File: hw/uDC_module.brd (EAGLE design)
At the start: 25 x 45 mm, 37 parts, among them J1 GROVE-4P-2.0-3470130P1, J2 GROVE-4P-2.0-3470130P1, U5 LD3985XX, X1 22-23-2021, X2 22-23-2021, X3 53047-06, X4 53047-06

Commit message: working on signal routin
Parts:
- added ZD1: (no value), dp_devices:SOD-323F
- moved C13 2.25 mm to (9.10, 22.9), turned to 0 degrees
- moved C18 0.30 mm to (5.80, 19.2)
- moved U5 0.20 mm to (5.80, 16.3)
- moved R2 0.10 mm to (12.7, 23.7)
- moved C15 0.10 mm to (11.3, 23.7)
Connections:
- removed net INV: U$7.P$7
- net !D2: now also U$6.33
- net !SF: now also U$6.31
- net D1: now also U$6.32
- net EN: now also U$6.18
- net FB: now also U$6.19, ZD1.C
- net GND: now also ZD1.A
- net IN1: now also U$6.26
- net IN2: now also U$6.29
- net SLEW: now also U$6.25
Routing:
- net !D2: track 0.00 -> 37.8 mm, vias 0 -> 2
- net D1: track 0.00 -> 28.6 mm, vias 0 -> 2
- net !SF: track 1.10 -> 29.7 mm, vias 1 -> 2
- net IN2: track 0.00 -> 12.2 mm, vias 0 -> 2
- net IN1: track 0.00 -> 10.4 mm
- net SLEW: track 0.00 -> 9.51 mm
- net EN: track 0.00 -> 8.76 mm
- net FB: track 3.25 -> 9.42 mm

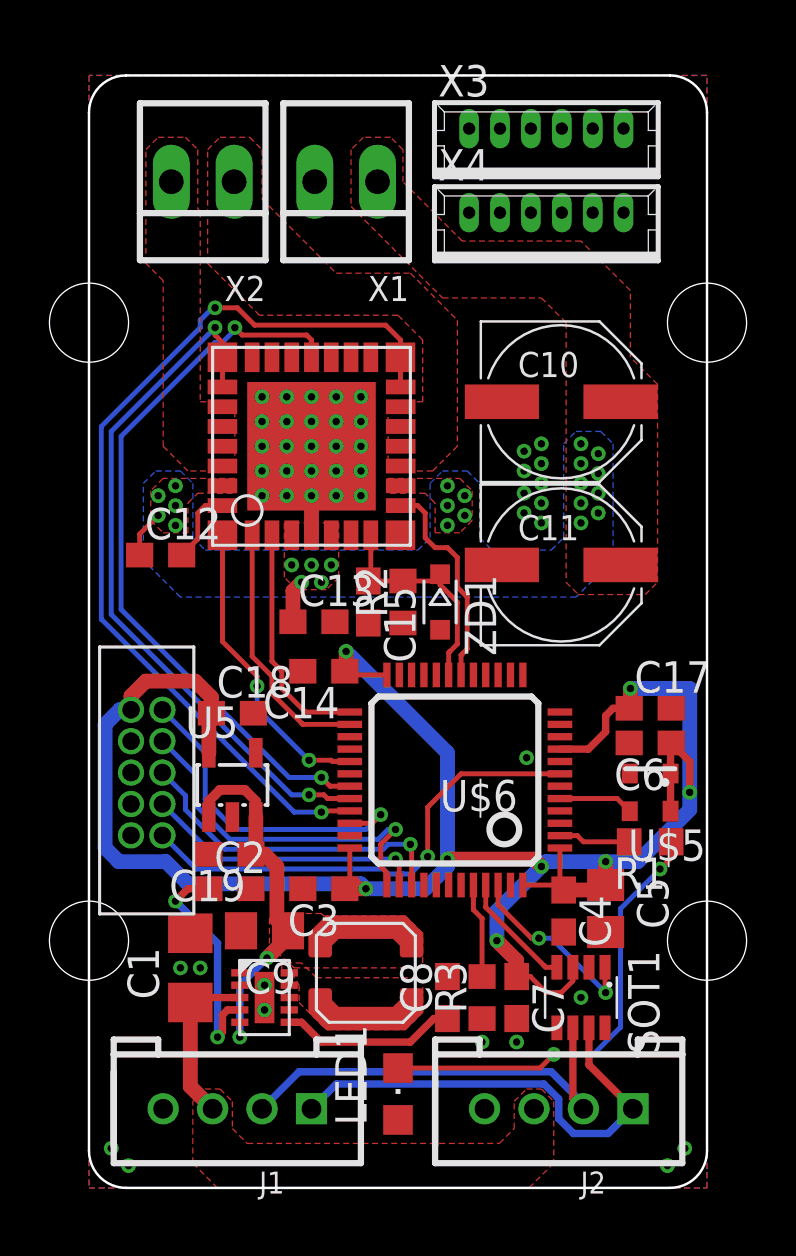
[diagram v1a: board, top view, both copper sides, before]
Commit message: routing encoder signals
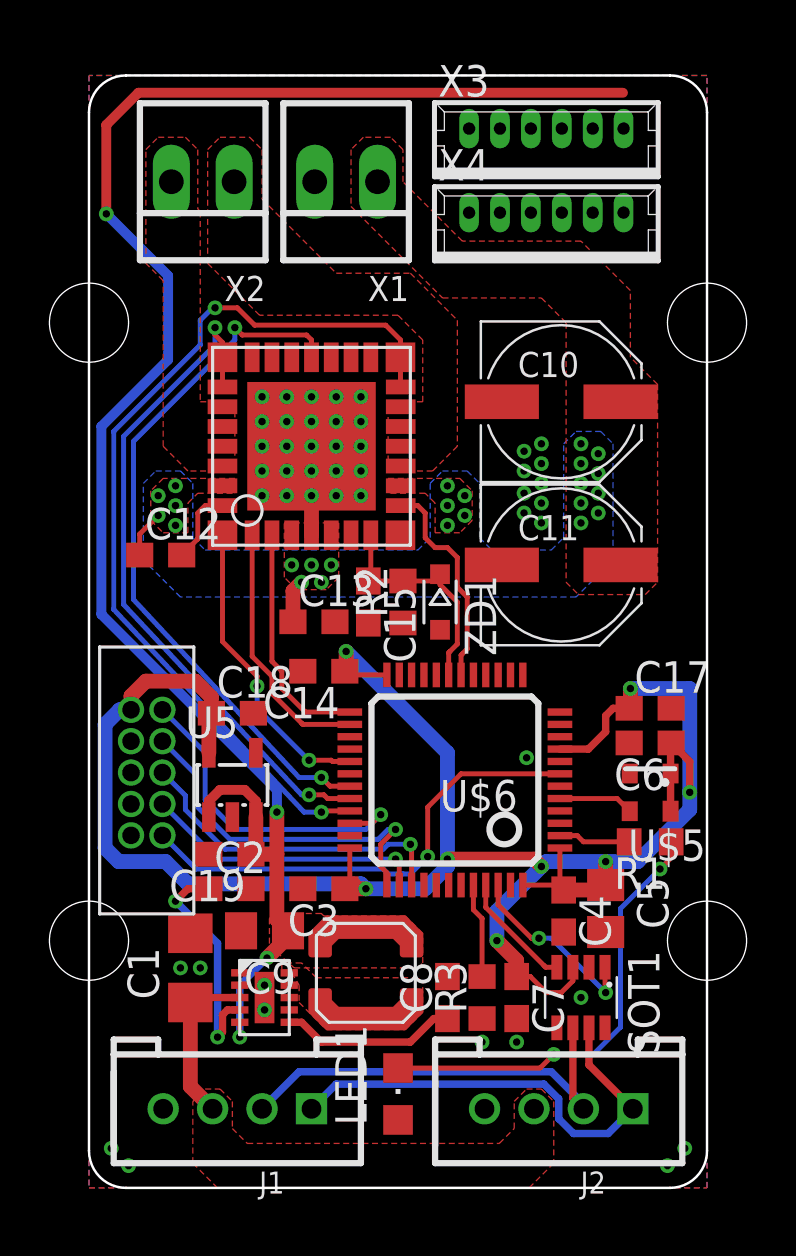
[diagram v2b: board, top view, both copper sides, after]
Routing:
- net +5V: track 14.9 -> 71.2 mm, vias 2 -> 4
- net !SF: track 29.7 -> 28.7 mm
- net !D2: track 37.8 -> 37.0 mm
- net D1: track 28.6 -> 27.8 mm
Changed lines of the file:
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@@
 <grid distance="0.5" unitdist="mm" unit="mm" style="dots" multiple="1" display="yes" altdistance="0.1" altunitdist="mm" altunit="mm"/>
 <layers>
-<layer number="1" name="Top" color="4" fill="1" visible="no" active="yes"/>
+<layer number="1" name="Top" color="4" fill="1" visible="yes" active="yes"/>
 <layer number="16" name="Bottom" color="1" fill="1" visible="yes" active="yes"/>
 <layer number="17" name="Pads" color="2" fill="1" visible="yes" active="yes"/>
@@
 <layer number="42" name="bRestrict" color="1" fill="10" visible="yes" active="yes"/>
 <layer number="43" name="vRestrict" color="2" fill="10" visible="no" active="yes"/>
-<layer number="44" name="Drills" color="7" fill="1" visible="no" active="yes"/>
-<layer number="45" name="Holes" color="7" fill="1" visible="yes" active="yes"/>
-<layer number="46" name="Milling" color="3" fill="1" visible="yes" active="yes"/>
+<layer number="44" name="Drills" color="7" fill="1" visible="yes" active="yes"/>
+<layer number="45" name="Holes" color="7" fill="1" visible="no" active="yes"/>
+<layer number="46" name="Milling" color="3" fill="1" visible="no" active="yes"/>
 <layer number="47" name="Measures" color="7" fill="1" visible="no" active="yes"/>
 <layer number="48" name="Document" color="7" fill="1" visible="no" active="yes"/>
@@
 <wire x1="10.55" y1="16.25" x2="9.75" y2="16.25" width="0.2" layer="1"/>
 <wire x1="9.75" y1="16.25" x2="9.4" y2="16.6" width="0.2" layer="1"/>
-<wire x1="1.3" y1="23.4" x2="1.3" y2="30.4" width="0.2" layer="16"/>
-<wire x1="1.3" y1="30.4" x2="5.1" y2="34.2" width="0.2" layer="16"/>
-<wire x1="5.9" y1="34.8" x2="5.9" y2="34.7" width="0.2" layer="16"/>
-<wire x1="5.9" y1="34.7" x2="5.4" y2="34.2" width="0.2" layer="16"/>
-<wire x1="5.4" y1="34.2" x2="5.1" y2="34.2" width="0.2" layer="16"/>
-<wire x1="1.3" y1="23.4" x2="8.1" y2="16.6" width="0.2" layer="16"/>
-<wire x1="8.1" y1="16.6" x2="9.4" y2="16.6" width="0.2" layer="16"/>
+<wire x1="1.8" y1="23.8" x2="1.8" y2="30.2" width="0.2" layer="16"/>
+<wire x1="1.8" y1="23.8" x2="8.5" y2="16.6" width="0.2" layer="16"/>
+<wire x1="8.5" y1="16.6" x2="9.4" y2="16.6" width="0.2" layer="16"/>
+<wire x1="1.8" y1="30.2" x2="5.9" y2="34.3" width="0.2" layer="16"/>
+<wire x1="5.9" y1="34.3" x2="5.9" y2="34.8" width="0.2" layer="16"/>
 </signal>
 <signal name="SLEW">
@@
 <wire x1="10.55" y1="15.25" x2="9.45" y2="15.25" width="0.2" layer="1"/>
 <wire x1="9.45" y1="15.25" x2="9.4" y2="15.2" width="0.2" layer="1"/>
-<wire x1="0.5" y1="30.8" x2="4.5" y2="34.8" width="0.2" layer="16"/>
-<wire x1="4.5" y1="34.8" x2="4.5" y2="35.1" width="0.2" layer="16"/>
-<wire x1="5.1" y1="35.6" x2="5" y2="35.6" width="0.2" layer="16"/>
-<wire x1="5" y1="35.6" x2="4.5" y2="35.1" width="0.2" layer="16"/>
-<wire x1="0.5" y1="23" x2="0.5" y2="30.8" width="0.2" layer="16"/>
-<wire x1="0.5" y1="23" x2="8.3" y2="15.2" width="0.2" layer="16"/>
-<wire x1="8.3" y1="15.2" x2="9.4" y2="15.2" width="0.2" layer="16"/>
+<wire x1="1" y1="23.4" x2="1" y2="30.6" width="0.2" layer="16"/>
+<wire x1="1" y1="23.4" x2="8.7" y2="15.2" width="0.2" layer="16"/>
+<wire x1="8.7" y1="15.2" x2="9.4" y2="15.2" width="0.2" layer="16"/>
+<wire x1="1" y1="30.6" x2="4.5" y2="34.1" width="0.2" layer="16"/>
+<wire x1="4.5" y1="34.1" x2="4.5" y2="35.1" width="0.2" layer="16"/>
+<wire x1="4.5" y1="35.1" x2="5" y2="35.6" width="0.2" layer="16"/>
+<wire x1="5" y1="35.6" x2="5.1" y2="35.6" width="0.2" layer="16"/>
 </signal>
 <signal name="IN2">
@@
 <wire x1="6.75" y1="15.65" x2="6.3" y2="16.1" width="0.4" layer="1"/>
 <wire x1="6.3" y1="16.1" x2="5.3" y2="16.1" width="0.4" layer="1"/>
-<wire x1="6.55" y1="13.5" x2="7.1" y2="13.5" width="0.6" layer="1"/>
-<wire x1="7.1" y1="13.5" x2="7.6" y2="13" width="0.6" layer="1"/>
-<wire x1="7.6" y1="13" x2="7.6" y2="10.85" width="0.6" layer="1"/>
 <wire x1="7.6" y1="10.85" x2="8.05" y2="10.4" width="0.6" layer="1"/>
+<wire x1="7.6" y1="10.85" x2="7.6" y2="13.5" width="0.6" layer="1"/>
+<via x="7.6" y="15.2" extent="1-16" drill="0.3"/>
+<wire x1="7.6" y1="13.5" x2="7.6" y2="15.2" width="0.6" layer="1"/>
+<wire x1="6.55" y1="13.5" x2="7.6" y2="13.5" width="0.6" layer="1"/>
+<wire x1="7.6" y1="15.2" x2="7.6" y2="16.1" width="0.4" layer="16"/>
+<wire x1="7.6" y1="16.1" x2="0.5" y2="23.2" width="0.4" layer="16"/>
+<wire x1="0.5" y1="23.2" x2="0.5" y2="30.8" width="0.4" layer="16"/>
+<wire x1="0.5" y1="30.8" x2="3.2" y2="33.5" width="0.4" layer="16"/>
+<wire x1="3.2" y1="33.5" x2="3.2" y2="36.9" width="0.4" layer="16"/>
+<wire x1="3.2" y1="36.9" x2="0.7" y2="39.4" width="0.4" layer="16"/>
+<via x="0.7" y="39.4" extent="1-16" drill="0.3"/>
+<wire x1="0.7" y1="39.4" x2="0.7" y2="43" width="0.4" layer="1"/>
+<wire x1="0.7" y1="43" x2="2" y2="44.3" width="0.4" layer="1"/>
+<wire x1="2" y1="44.3" x2="21.6" y2="44.3" width="0.4" layer="1"/>
 </signal>
 <signal name="D1">
@@
 <wire x1="9.65" y1="15.75" x2="9.5" y2="15.9" width="0.2" layer="1"/>
 <wire x1="9.5" y1="15.9" x2="8.9" y2="15.9" width="0.2" layer="1"/>
-<wire x1="0.9" y1="23.2" x2="0.9" y2="30.6" width="0.2" layer="16"/>
-<wire x1="0.9" y1="30.6" x2="5.1" y2="34.8" width="0.2" layer="16"/>
-<wire x1="0.9" y1="23.2" x2="8.2" y2="15.9" width="0.2" layer="16"/>
-<wire x1="8.2" y1="15.9" x2="8.9" y2="15.9" width="0.2" layer="16"/>
+<wire x1="1.4" y1="23.6" x2="1.4" y2="30.4" width="0.2" layer="16"/>
+<wire x1="1.4" y1="23.6" x2="8.6" y2="15.9" width="0.2" layer="16"/>
+<wire x1="8.6" y1="15.9" x2="8.9" y2="15.9" width="0.2" layer="16"/>
+<wire x1="1.4" y1="30.4" x2="5.1" y2="34.1" width="0.2" layer="16"/>
+<wire x1="5.1" y1="34.1" x2="5.1" y2="34.8" width="0.2" layer="16"/>
 </signal>
 </signals>

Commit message: layout completed
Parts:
- moved X3 3.40 mm to (18.5, 39.0)
- moved X4 3.40 mm to (18.5, 42.4)
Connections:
- new net ANALOG: U$6.12, X4.6
- new net ENC_A: U$6.42, X4.3
- new net ENC_B: U$6.43, X4.4
- new net ENC_I: U$6.41, X4.5
- new net LIMIT_A: U$6.13, X3.1
- new net LIMIT_B: U$6.14, X3.3
- new net STOP: U$6.15, X3.5
- net +5V: now also X4.1
- net GND: now also X3.2, X3.4, X3.6, X4.2
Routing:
- net ENC_B: track 0.00 -> 45.7 mm, vias 0 -> 1
- net ENC_I: track 0.00 -> 44.1 mm, vias 0 -> 1
- net ENC_A: track 0.00 -> 43.7 mm, vias 0 -> 1
- net ANALOG: track 0.00 -> 34.6 mm, vias 0 -> 1
- net STOP: track 0.00 -> 26.0 mm, vias 0 -> 1
- net LIMIT_B: track 0.00 -> 25.9 mm, vias 0 -> 1
- net LIMIT_A: track 0.00 -> 25.0 mm, vias 0 -> 1
- net +3V3: track 86.7 -> 83.3 mm
- net +5V: track 71.2 -> 72.3 mm
- net GND: vias 46 -> 53
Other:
- board text added: "ENC"
- board text added: "MOTOR"
- board text added: "STOP"
- board text added: "SUPPLY"

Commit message: updated all connectors to have GND on pin 1
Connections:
- net +5V: now also X4.2; no longer X4.1
- net GND: now also X3.1, X3.3, X3.5, X4.1; no longer X3.2, X3.4, X3.6, X4.2
- net LIMIT_A: now also X3.2; no longer X3.1
- net LIMIT_B: now also X3.4; no longer X3.3
- net STOP: now also X3.6; no longer X3.5
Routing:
- net +5V: track 72.3 -> 71.1 mm
- net LIMIT_A: track 25.0 -> 24.4 mm
- net STOP: track 26.0 -> 26.5 mm
- net LIMIT_B: track 25.9 -> 26.4 mm
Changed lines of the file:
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@@
 <grid distance="0.5" unitdist="mm" unit="mm" style="dots" multiple="1" display="yes" altdistance="0.1" altunitdist="mm" altunit="mm"/>
 <layers>
-<layer number="1" name="Top" color="4" fill="1" visible="yes" active="yes"/>
-<layer number="16" name="Bottom" color="1" fill="1" visible="no" active="yes"/>
+<layer number="1" name="Top" color="4" fill="1" visible="no" active="yes"/>
+<layer number="16" name="Bottom" color="1" fill="1" visible="yes" active="yes"/>
 <layer number="17" name="Pads" color="2" fill="1" visible="yes" active="yes"/>
 <layer number="18" name="Vias" color="2" fill="1" visible="yes" active="yes"/>
 <layer number="19" name="Unrouted" color="6" fill="1" visible="yes" active="yes"/>
 <layer number="20" name="Dimension" color="15" fill="1" visible="yes" active="yes"/>
-<layer number="21" name="tPlace" color="7" fill="1" visible="yes" active="yes"/>
-<layer number="22" name="bPlace" color="7" fill="1" visible="no" active="yes"/>
-<layer number="23" name="tOrigins" color="15" fill="1" visible="yes" active="yes"/>
-<layer number="24" name="bOrigins" color="15" fill="1" visible="no" active="yes"/>
+<layer number="21" name="tPlace" color="7" fill="1" visible="no" active="yes"/>
+<layer number="22" name="bPlace" color="7" fill="1" visible="yes" active="yes"/>
+<layer number="23" name="tOrigins" color="15" fill="1" visible="no" active="yes"/>
+<layer number="24" name="bOrigins" color="15" fill="1" visible="yes" active="yes"/>
 <layer number="25" name="tNames" color="7" fill="1" visible="no" active="yes"/>
 <layer number="26" name="bNames" color="7" fill="1" visible="no" active="yes"/>
@@
 <layer number="37" name="tTest" color="7" fill="1" visible="no" active="yes"/>
 <layer number="38" name="bTest" color="7" fill="1" visible="no" active="yes"/>
-<layer number="39" name="tKeepout" color="4" fill="11" visible="yes" active="yes"/>
-<layer number="40" name="bKeepout" color="1" fill="11" visible="no" active="yes"/>
-<layer number="41" name="tRestrict" color="4" fill="10" visible="yes" active="yes"/>
-<layer number="42" name="bRestrict" color="1" fill="10" visible="no" active="yes"/>
+<layer number="39" name="tKeepout" color="4" fill="11" visible="no" active="yes"/>
+<layer number="40" name="bKeepout" color="1" fill="11" visible="yes" active="yes"/>
+<layer number="41" name="tRestrict" color="4" fill="10" visible="no" active="yes"/>
+<layer number="42" name="bRestrict" color="1" fill="10" visible="yes" active="yes"/>
 <layer number="43" name="vRestrict" color="2" fill="10" visible="no" active="yes"/>
 <layer number="44" name="Drills" color="7" fill="1" visible="no" active="yes"/>
@@
 <layer number="46" name="Milling" color="3" fill="1" visible="yes" active="yes"/>
 <layer number="47" name="Measures" color="7" fill="1" visible="no" active="yes"/>
-<layer number="48" name="Document" color="7" fill="1" visible="yes" active="yes"/>
+<layer number="48" name="Document" color="7" fill="1" visible="no" active="yes"/>
 <layer number="49" name="Reference" color="7" fill="1" visible="no" active="yes"/>
 <layer number="50" name="dxf" color="7" fill="1" visible="no" active="no"/>
-<layer number="51" name="tDocu" color="7" fill="1" visible="yes" active="yes"/>
-<layer number="52" name="bDocu" color="7" fill="1" visible="no" active="yes"/>
+<layer number="51" name="tDocu" color="7" fill="1" visible="no" active="yes"/>
+<layer number="52" name="bDocu" color="7" fill="1" visible="yes" active="yes"/>
 <layer number="53" name="tGND_GNDA" color="7" fill="1" visible="no" active="no"/>
 <layer number="54" name="bGND_GNDA" color="7" fill="1" visible="no" active="no"/>
@@
 <wire x1="9" y1="26.4" x2="9" y2="28" width="0.6" layer="1"/>
 <contactref element="ZD1" pad="A"/>
-<contactref element="X4" pad="2"/>
-<contactref element="X3" pad="2"/>
-<contactref element="X3" pad="4"/>
-<contactref element="X3" pad="6"/>
 <via x="4.5" y="23.2" extent="1-16" drill="0.3"/>
 <via x="4.5" y="22.2" extent="1-16" drill="0.3"/>
@@
 <via x="17.3" y="22.9" extent="1-16" drill="0.3"/>
 <via x="18.1" y="11.2" extent="1-16" drill="0.3"/>
+<contactref element="X4" pad="1"/>
+<contactref element="X3" pad="1"/>
+<contactref element="X3" pad="3"/>
+<contactref element="X3" pad="5"/>
 </signal>
 <signal name="VIN">
@@
 <wire x1="0.7" y1="39.4" x2="0.7" y2="43" width="0.4" layer="1"/>
 <wire x1="0.7" y1="43" x2="2" y2="44.3" width="0.4" layer="1"/>
-<wire x1="2" y1="44.3" x2="20.1" y2="44.3" width="0.4" layer="1"/>
-<contactref element="X4" pad="1"/>
-<wire x1="20.1" y1="44.3" x2="21" y2="44.3" width="0.4" layer="1"/>
-<wire x1="21.625" y1="42.85" x2="21.625" y2="43.675" width="0.4" layer="1"/>
-<wire x1="21.625" y1="43.675" x2="21" y2="44.3" width="0.4" layer="1"/>
+<contactref element="X4" pad="2"/>
+<wire x1="20.375" y1="42.85" x2="20.375" y2="43.625" width="0.4" layer="1"/>
+<wire x1="20.375" y1="43.625" x2="19.7" y2="44.3" width="0.4" layer="1"/>
+<wire x1="19.7" y1="44.3" x2="2" y2="44.3" width="0.4" layer="1"/>
 </signal>
 <signal name="D1">
@@
 </signal>
 <signal name="STOP">
-<contactref element="X3" pad="5"/>
 <contactref element="U$6" pad="15"/>
 <via x="16.3" y="19.7" extent="1-16" drill="0.3"/>
 <wire x1="16.55" y1="20.75" x2="16.55" y2="19.95" width="0.2" layer="1"/>
 <wire x1="16.55" y1="19.95" x2="16.3" y2="19.7" width="0.2" layer="1"/>
-<wire x1="16.625" y1="39.45" x2="16.625" y2="38.675" width="0.2" layer="16"/>
-<wire x1="16.625" y1="38.675" x2="19.4" y2="35.9" width="0.2" layer="16"/>
-<wire x1="19.4" y1="35.9" x2="19.4" y2="32.5" width="0.2" layer="16"/>
 <wire x1="19.4" y1="32.5" x2="22.1" y2="29.8" width="0.2" layer="16"/>
 <wire x1="22.1" y1="29.8" x2="22.1" y2="24.9" width="0.2" layer="16"/>
@@
 <wire x1="16.3" y1="19.8" x2="17.2" y2="20.7" width="0.2" layer="16"/>
 <wire x1="17.2" y1="20.7" x2="17.9" y2="20.7" width="0.2" layer="16"/>
+<contactref element="X3" pad="6"/>
+<wire x1="19.4" y1="32.5" x2="19.4" y2="34.6" width="0.2" layer="16"/>
+<wire x1="15.375" y1="39.45" x2="15.375" y2="38.625" width="0.2" layer="16"/>
+<wire x1="15.375" y1="38.625" x2="19.4" y2="34.6" width="0.2" layer="16"/>
 </signal>
 <signal name="LIMIT_B">
-<contactref element="X3" pad="3"/>
 <contactref element="U$6" pad="14"/>
 <via x="17" y="19.2" extent="1-16" drill="0.3"/>
 <wire x1="17.05" y1="20.75" x2="17.05" y2="19.25" width="0.2" layer="1"/>
 <wire x1="17.05" y1="19.25" x2="17" y2="19.2" width="0.2" layer="1"/>
-<wire x1="19.125" y1="39.45" x2="19.125" y2="38.675" width="0.2" layer="16"/>
-<wire x1="19.125" y1="38.675" x2="19.8" y2="38" width="0.2" layer="16"/>
-<wire x1="19.8" y1="38" x2="19.8" y2="32.7" width="0.2" layer="16"/>
 <wire x1="19.8" y1="32.7" x2="22.5" y2="30" width="0.2" layer="16"/>
 <wire x1="17" y1="19.2" x2="17" y2="19.9" width="0.2" layer="16"/>
@@
 <wire x1="18.1" y1="20.3" x2="22.5" y2="24.7" width="0.2" layer="16"/>
 <wire x1="22.5" y1="24.7" x2="22.5" y2="30" width="0.2" layer="16"/>
+<contactref element="X3" pad="4"/>
+<wire x1="19.8" y1="32.7" x2="19.8" y2="36.7" width="0.2" layer="16"/>
+<wire x1="17.875" y1="39.45" x2="17.875" y2="38.625" width="0.2" layer="16"/>
+<wire x1="17.875" y1="38.625" x2="19.8" y2="36.7" width="0.2" layer="16"/>
 </signal>
 <signal name="LIMIT_A">
-<contactref element="X3" pad="1"/>
 <contactref element="U$6" pad="13"/>
 <via x="17.7" y="19.7" extent="1-16" drill="0.3"/>
 <wire x1="17.55" y1="20.75" x2="17.55" y2="19.85" width="0.2" layer="1"/>
 <wire x1="17.55" y1="19.85" x2="17.7" y2="19.7" width="0.2" layer="1"/>
-<wire x1="21.625" y1="39.45" x2="21.625" y2="38.525" width="0.2" layer="16"/>
-<wire x1="21.625" y1="38.525" x2="20.2" y2="37.1" width="0.2" layer="16"/>
-<wire x1="20.2" y1="37.1" x2="20.2" y2="32.9" width="0.2" layer="16"/>
 <wire x1="20.2" y1="32.9" x2="22.9" y2="30.2" width="0.2" layer="16"/>
 <wire x1="17.7" y1="19.7" x2="18.1" y2="19.7" width="0.2" layer="16"/>
 <wire x1="18.1" y1="19.7" x2="22.9" y2="24.5" width="0.2" layer="16"/>
 <wire x1="22.9" y1="24.5" x2="22.9" y2="30.2" width="0.2" layer="16"/>
+<contactref element="X3" pad="2"/>
+<wire x1="20.2" y1="32.9" x2="20.2" y2="38.4" width="0.2" layer="16"/>
+<wire x1="20.375" y1="39.45" x2="20.375" y2="38.575" width="0.2" layer="16"/>
+<wire x1="20.375" y1="38.575" x2="20.2" y2="38.4" width="0.2" layer="16"/>
 </signal>
 </signals>
